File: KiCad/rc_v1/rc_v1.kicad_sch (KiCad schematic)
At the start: 33 parts, among them SW1 OS102011MS2Qxxx, SW10 TS12-1212, SW3 TS12-66, SW4 TS12-66, SW5 TS12-66, SW6 TS12-66, SW7 TS12-66, SW8 TS12-66, SW9 TS12-1212, U1 SDTx39xx2W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

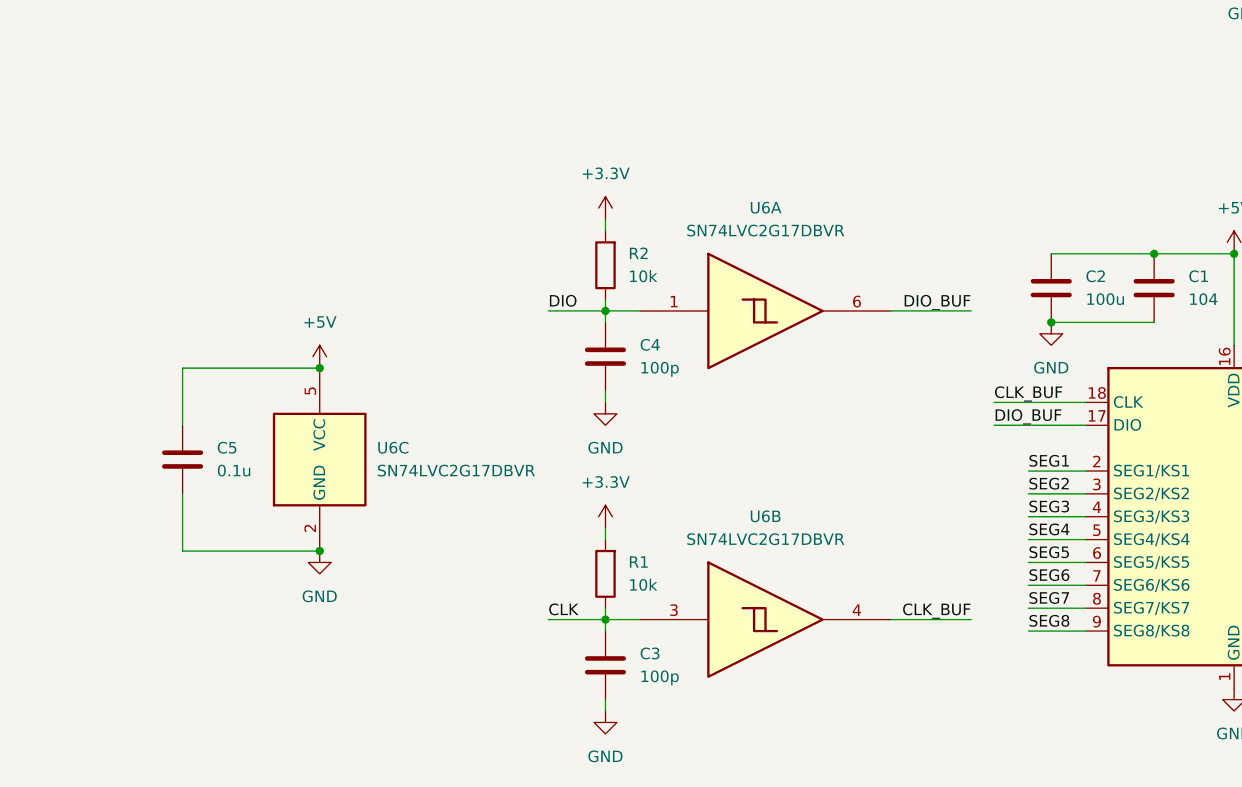
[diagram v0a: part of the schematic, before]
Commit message: Remote Controller PCB Milestone 5
Added level shifter IC, prototype board nearly completed
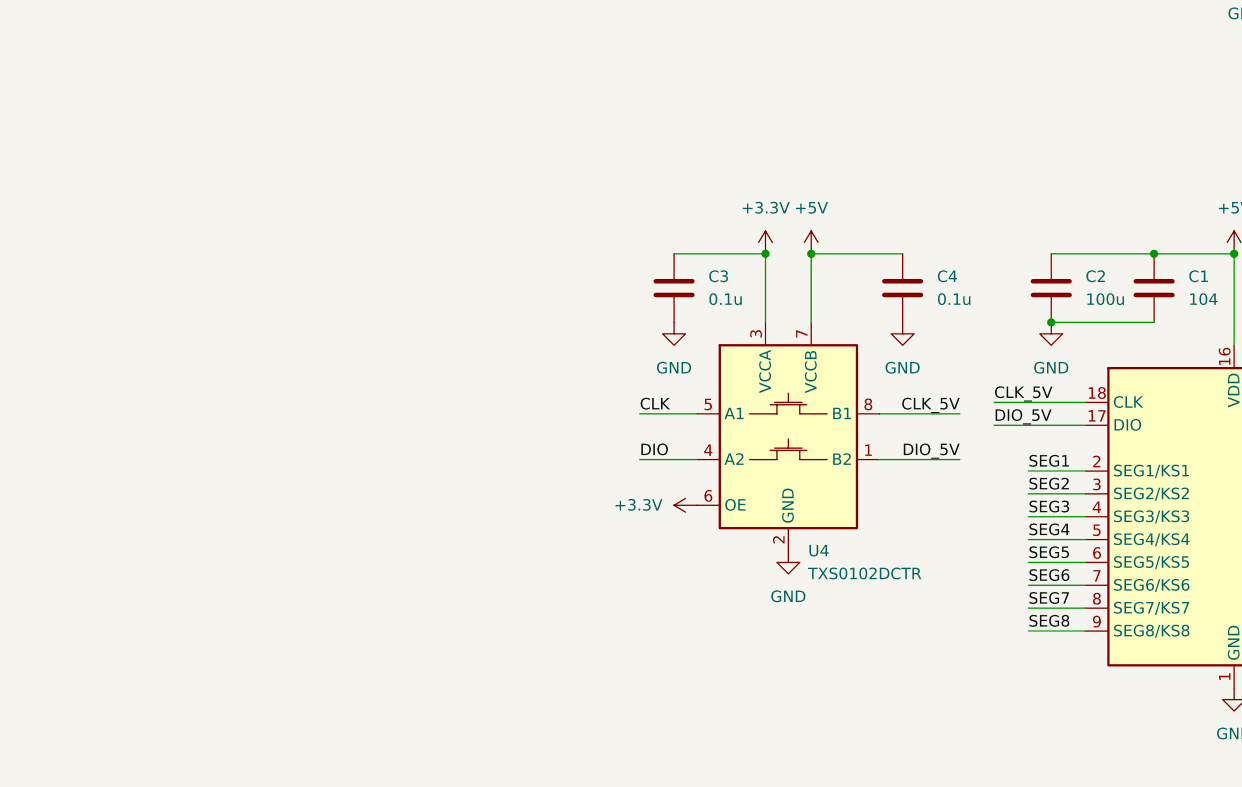
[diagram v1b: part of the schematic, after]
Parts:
- removed C5: 0.1u, Capacitor_SMD:C_0603_1608Metric_Pad1.08x0.95mm_HandSolder, symbol Device:C
- removed R1, R2: 10k, Resistor_SMD:R_0603_1608Metric_Pad0.98x0.95mm_HandSolder, symbol Device:R
- removed U6: SN74LVC2G17DBVR, Footprint Library:SOT-23-6_HandSoldering_Rounded, symbol 74xGxx:74LVC2G17
- added U4: TXS0102DCTR, Footprint Library:SSOP-8_2.95x2.8mm_P0.65mm, symbol Logic_LevelTranslator:TXS0102DCT
- C3, C4: value 100p -> 0.1u
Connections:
- net +3.3V: now also C3.1, U4.3 (VCCA), U4.6 (OE)
- net +5V: now also C4.1, U4.7 (VCCB)
- net CLK: now also U4.5 (A1); no longer C3.1
- net DIO: now also U4.4 (A2); no longer C4.1
- net GND: now also U4.2 (GND)
- net CLK_BUF renamed CLK_5V
- net CLK_5V: now also U4.8 (B1)
- net DIO_BUF renamed DIO_5V
- net DIO_5V: now also U4.1 (B2)

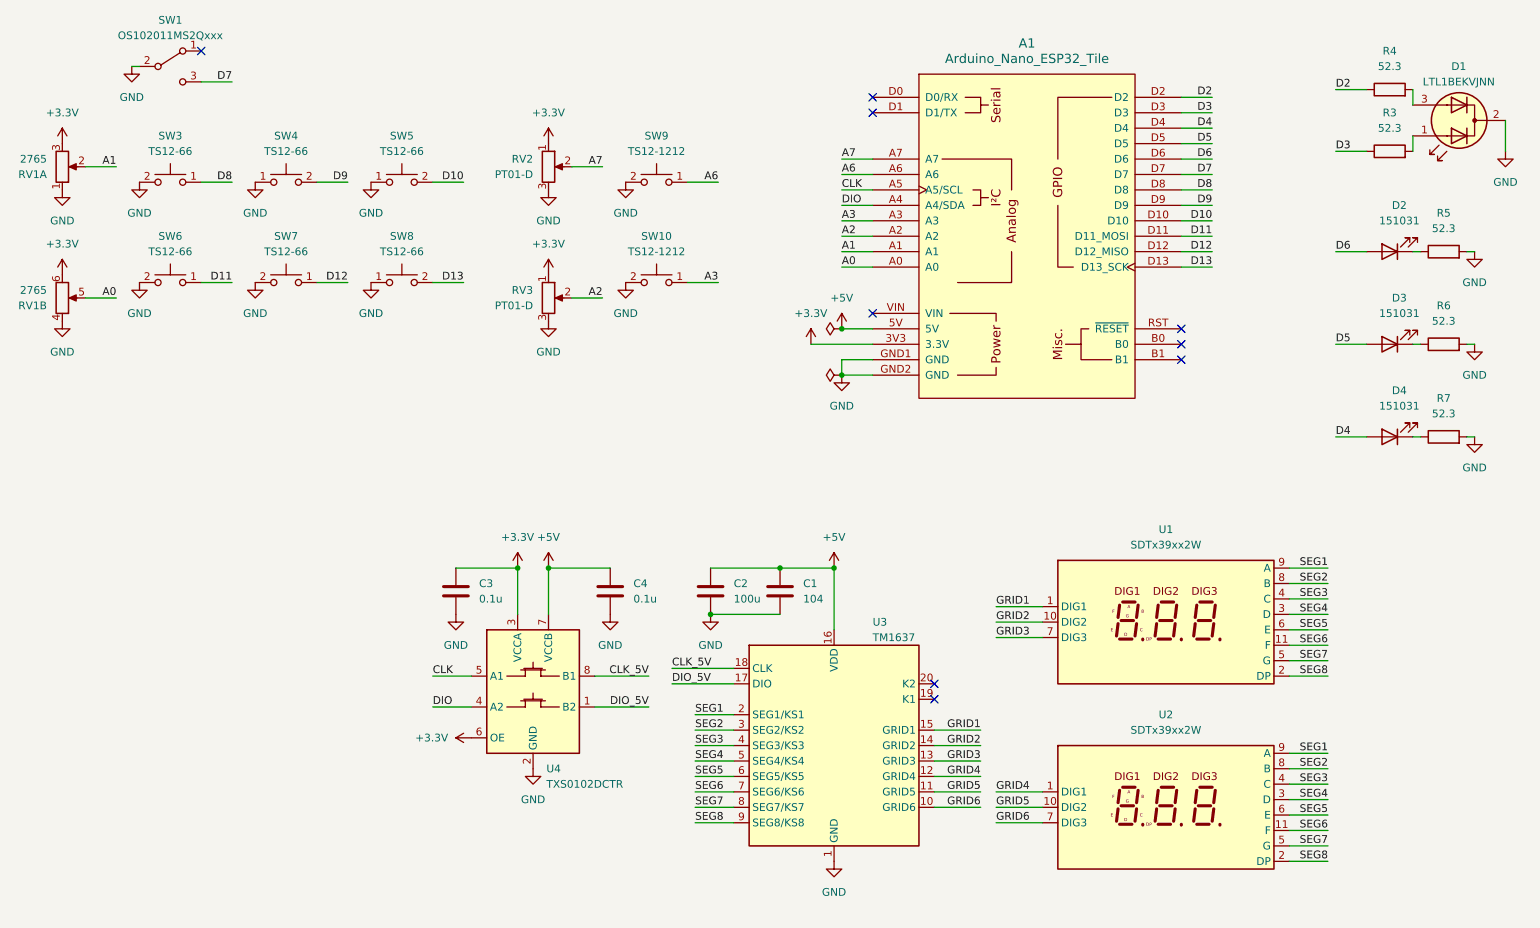
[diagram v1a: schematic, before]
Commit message: Remote Controller PCB Milestone 6
Added GPIO output to OE input pin
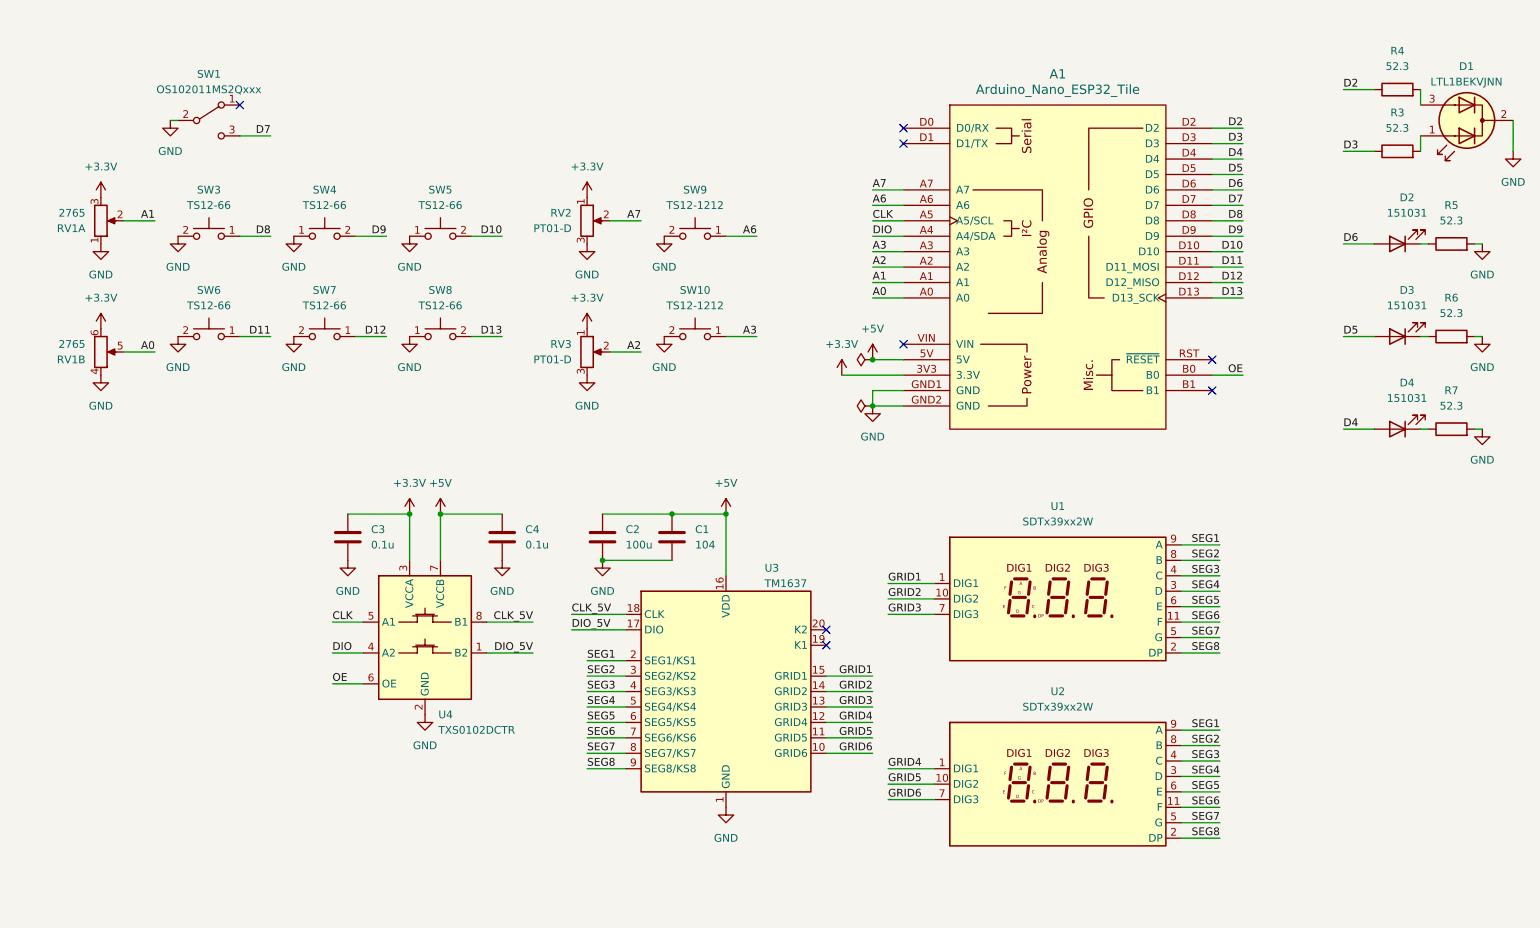
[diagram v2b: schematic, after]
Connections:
- net +3.3V: no longer U4.6 (OE)
- net OE: now reaches A1.B0
- net OE: now also U4.6 (OE)
- no-connect marks 9 -> 8
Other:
- moved on the sheet: A1, C1, C2, C3, C4, D1, D2, D3, D4, R3, R4, R5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
